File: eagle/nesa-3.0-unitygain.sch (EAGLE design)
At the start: 15 parts, among them IC1 OPA4134

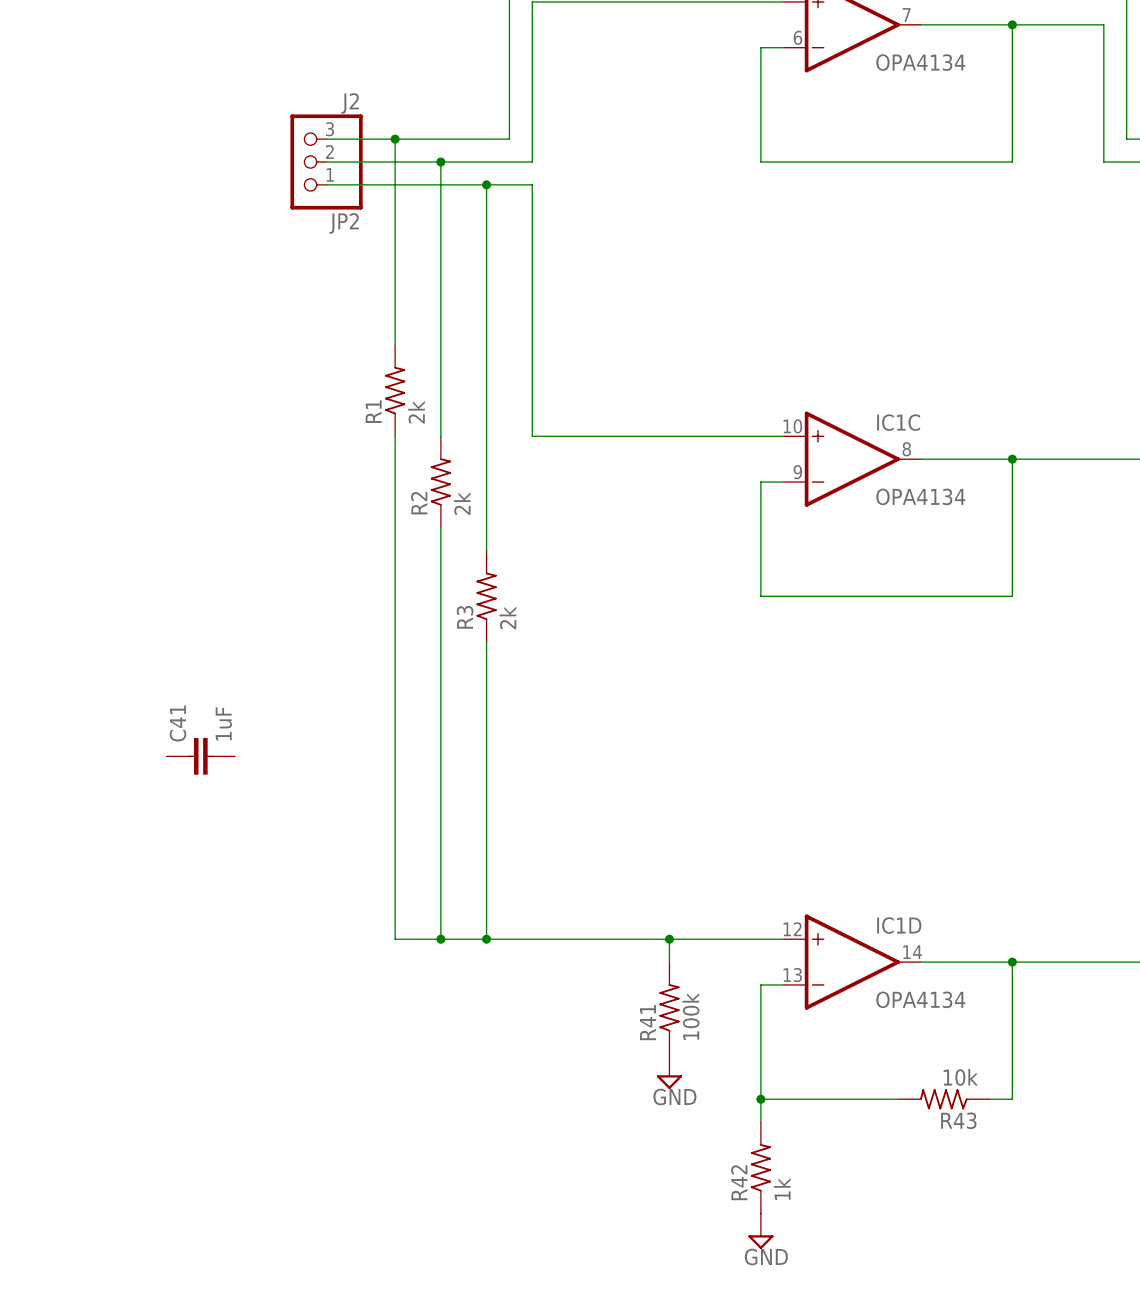
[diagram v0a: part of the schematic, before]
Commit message: Some minor changes to unitygain schematics
Don't use these schematics yet :)
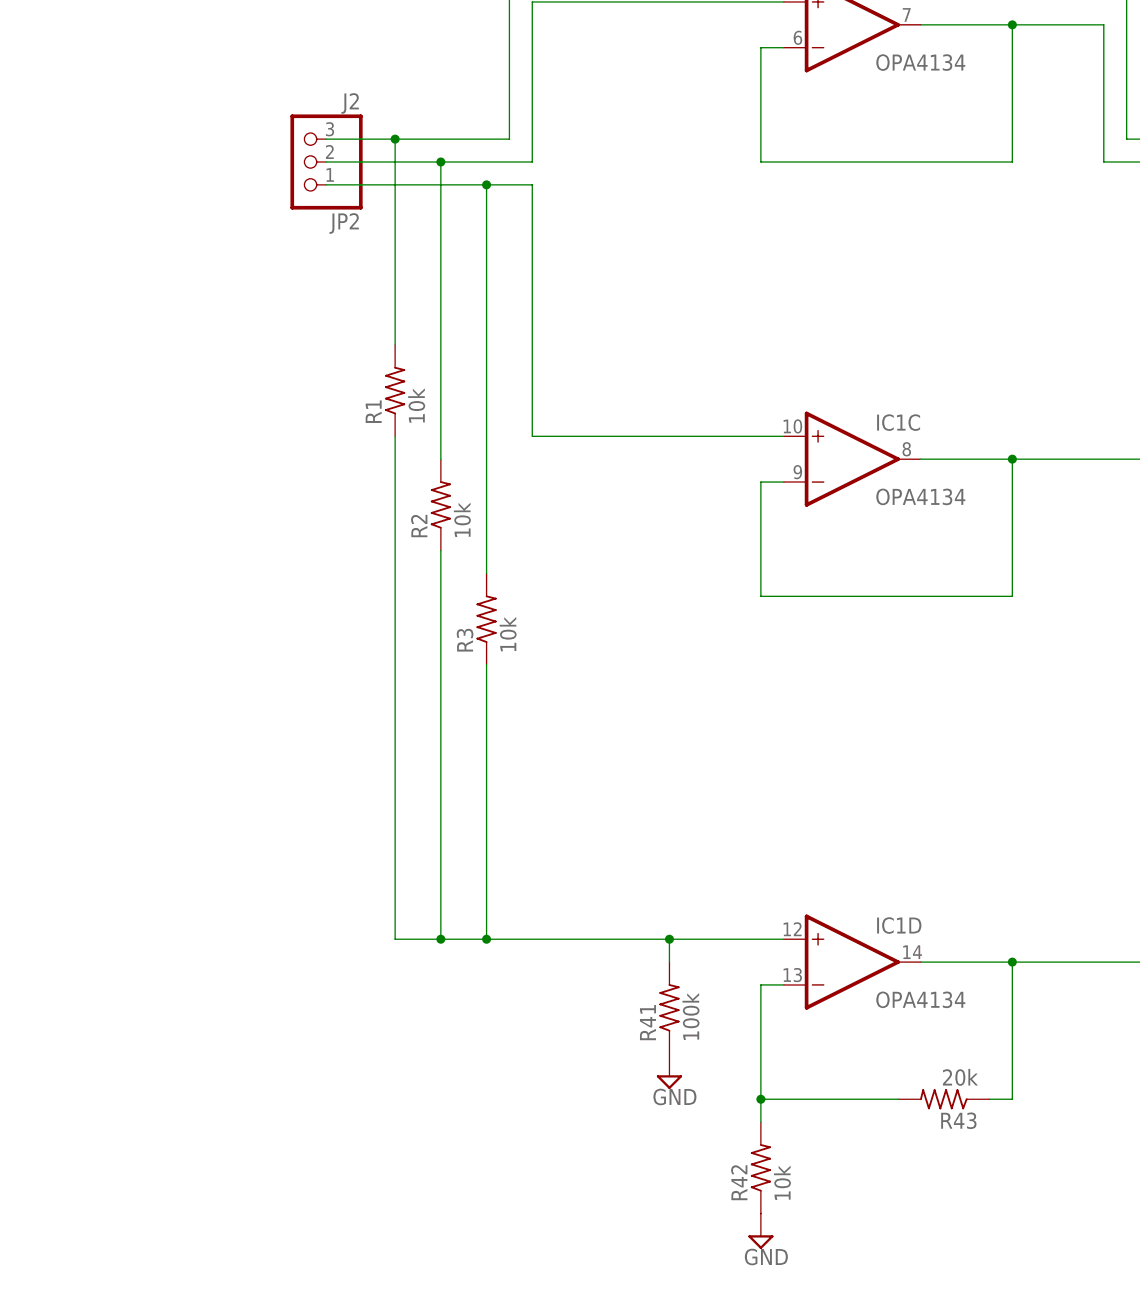
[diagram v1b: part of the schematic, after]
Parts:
- removed C41: 1uF, capacitor-wima:C5/7.2
- R1, R2, R3: value 2k -> 10k
- R42: value 1k -> 10k
- R43: value 10k -> 20k
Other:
- moved on the sheet: R2, R3
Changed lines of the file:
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@@
 <part name="JP2" library="pinhead" deviceset="PINHD-1X3" device="" value="J2"/>
 <part name="SUPPLY14" library="supply2" deviceset="GND" device=""/>
-<part name="C41" library="capacitor-wima" deviceset="C" device="5/7.2" value="1uF"/>
 <part name="R41" library="resistor" deviceset="R-US_" device="0204/7" value="100k"/>
 <part name="SUPPLY16" library="supply2" deviceset="GND" device=""/>
-<part name="R42" library="resistor" deviceset="R-US_" device="0204/7" value="1k"/>
+<part name="R42" library="resistor" deviceset="R-US_" device="0204/7" value="10k"/>
 <part name="SUPPLY17" library="supply2" deviceset="GND" device=""/>
-<part name="R43" library="resistor" deviceset="R-US_" device="0204/7" value="10k"/>
+<part name="R43" library="resistor" deviceset="R-US_" device="0204/7" value="20k"/>
 <part name="JP3" library="pinhead" deviceset="PINHD-2X4" device=""/>
-<part name="R1" library="resistor" deviceset="R-US_" device="0204/7" value="2k"/>
-<part name="R2" library="resistor" deviceset="R-US_" device="0204/7" value="2k"/>
-<part name="R3" library="resistor" deviceset="R-US_" device="0204/7" value="2k"/>
+<part name="R1" library="resistor" deviceset="R-US_" device="0204/7" value="10k"/>
+<part name="R2" library="resistor" deviceset="R-US_" device="0204/7" value="10k"/>
+<part name="R3" library="resistor" deviceset="R-US_" device="0204/7" value="10k"/>
 </parts>
 <sheets>
@@
 <instance part="SUPPLY14" gate="GND" x="147.32" y="-25.4"/>
 <instance part="IC1" gate="D" x="83.82" y="-101.6"/>
-<instance part="C41" gate="G$1" x="10.16" y="-78.74" rot="R90"/>
 <instance part="R41" gate="G$1" x="63.5" y="-106.68" rot="R90"/>
 <instance part="SUPPLY16" gate="GND" x="63.5" y="-114.3"/>
@@
 <instance part="JP3" gate="A" x="132.08" y="-15.24"/>
 <instance part="R1" gate="G$1" x="33.02" y="-38.1" rot="R90"/>
-<instance part="R2" gate="G$1" x="38.1" y="-48.26" rot="R90"/>
-<instance part="R3" gate="G$1" x="43.18" y="-60.96" rot="R90"/>
+<instance part="R2" gate="G$1" x="38.1" y="-50.8" rot="R90"/>
+<instance part="R3" gate="G$1" x="43.18" y="-63.5" rot="R90"/>
 </instances>
 <busses>
@@
 <pinref part="JP2" gate="A" pin="1"/>
 <pinref part="R3" gate="G$1" pin="2"/>
-<wire x1="43.18" y1="-55.88" x2="43.18" y2="-15.24" width="0.1524" layer="91"/>
+<wire x1="43.18" y1="-58.42" x2="43.18" y2="-15.24" width="0.1524" layer="91"/>
 <junction x="43.18" y="-15.24"/>
 <wire x1="76.2" y1="-43.18" x2="48.26" y2="-43.18" width="0.1524" layer="91"/>
@@
 <pinref part="JP2" gate="A" pin="2"/>
 <pinref part="R2" gate="G$1" pin="2"/>
-<wire x1="38.1" y1="-43.18" x2="38.1" y2="-12.7" width="0.1524" layer="91"/>
+<wire x1="38.1" y1="-45.72" x2="38.1" y2="-12.7" width="0.1524" layer="91"/>
 <junction x="38.1" y="-12.7"/>
 <pinref part="IC1" gate="B" pin="+IN"/>
@@
 <pinref part="R2" gate="G$1" pin="1"/>
 <wire x1="38.1" y1="-99.06" x2="43.18" y2="-99.06" width="0.1524" layer="91"/>
-<wire x1="38.1" y1="-53.34" x2="38.1" y2="-99.06" width="0.1524" layer="91"/>
+<wire x1="38.1" y1="-55.88" x2="38.1" y2="-99.06" width="0.1524" layer="91"/>
 <pinref part="R3" gate="G$1" pin="1"/>
-<wire x1="43.18" y1="-66.04" x2="43.18" y2="-99.06" width="0.1524" layer="91"/>
+<wire x1="43.18" y1="-68.58" x2="43.18" y2="-99.06" width="0.1524" layer="91"/>
 <junction x="38.1" y="-99.06"/>
 <pinref part="R41" gate="G$1" pin="2"/>
